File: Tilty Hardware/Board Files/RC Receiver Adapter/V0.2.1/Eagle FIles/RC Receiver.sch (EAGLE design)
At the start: 31 parts, among them U1 ATMEGA328P, U2 LM2931, U3 AP7313SOT23R, Y1 16MHz

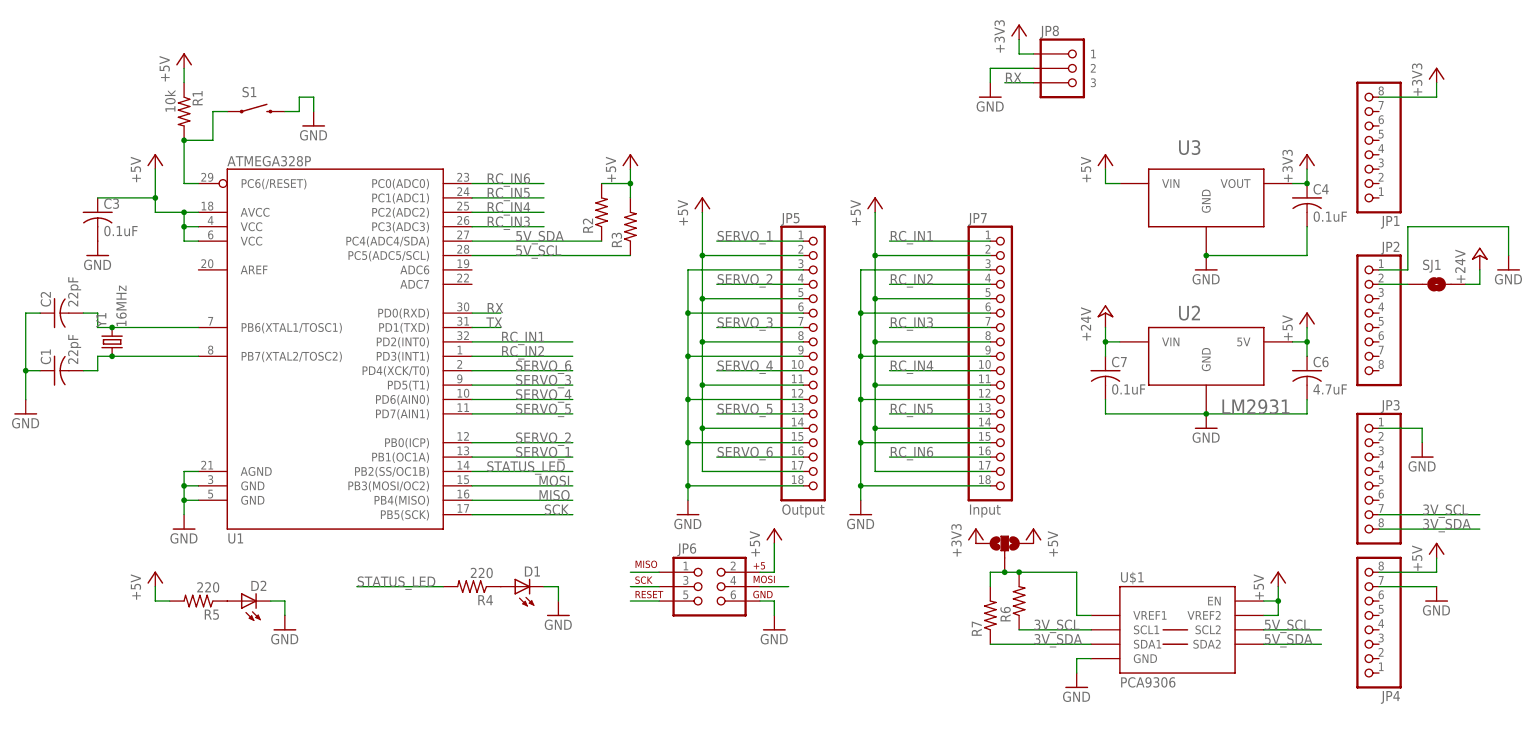
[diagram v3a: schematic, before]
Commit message: Updated RC adapter
Changed to use locking headers, 3v3 I2C line with level
translator/buffer, moved LEDs
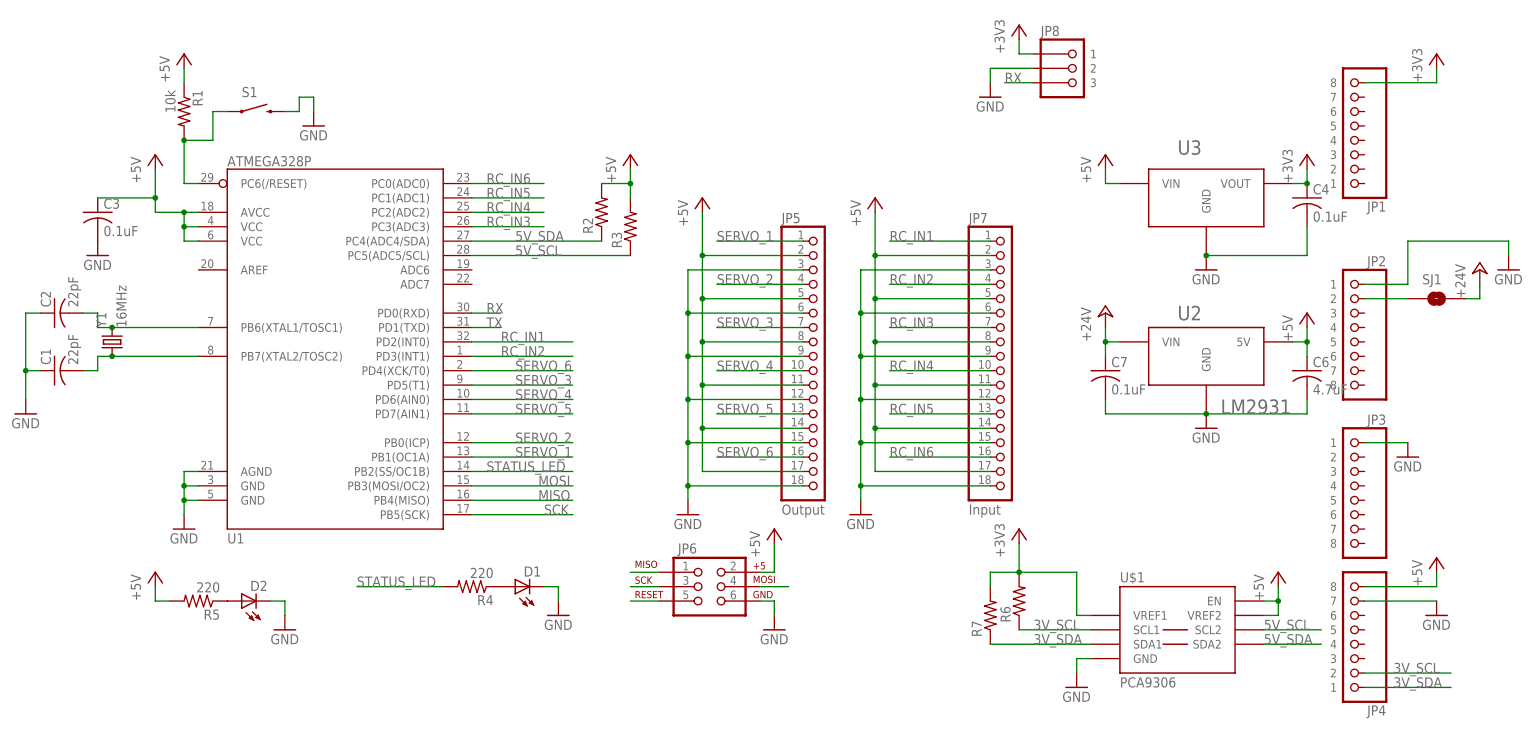
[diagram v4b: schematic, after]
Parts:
- removed SJ2: (no value), SparkFun-Passives:SOLDERJUMPER_2WAYS
- JP1, JP2, JP3, JP4: value (none) -> 8-PIN_HEADER; device pinhead:PINHD-1X81X08_NO_SILK -> My Parts:8-PIN_HEADER
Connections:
- removed net N$7: R6.2, R7.2, SJ2.2, U$1.VREF1
- net +3V3: now also R6.2, R7.2, U$1.VREF1; no longer SJ2.1
- net +5V: no longer SJ2.3
- net 3V_SCL: now also JP4.2; no longer JP3.7
- net 3V_SDA: now also JP4.1; no longer JP3.8
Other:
- moved on the sheet: SJ1

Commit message: Added Tilty silkscreen and option 5/3.3v I2C connections
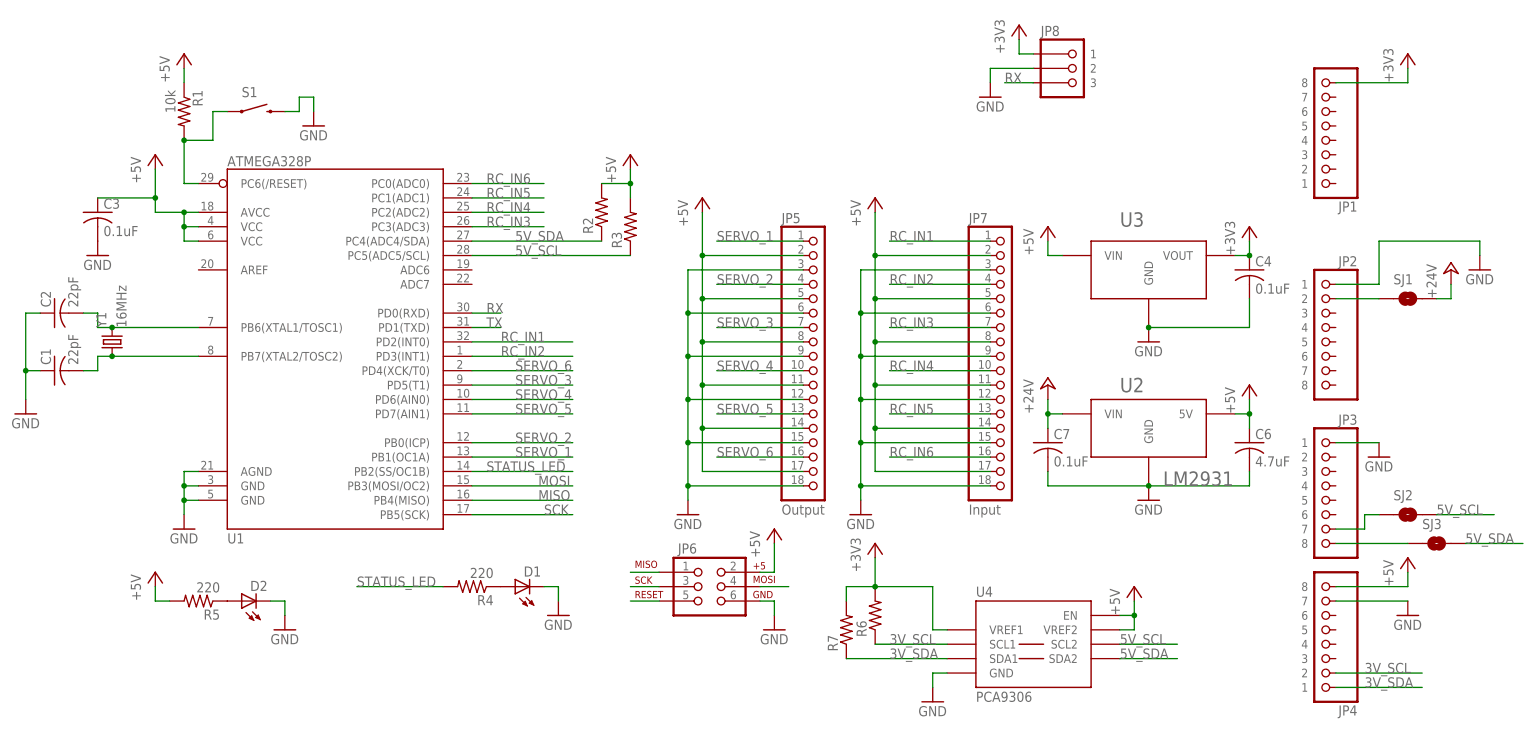
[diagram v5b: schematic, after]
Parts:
- removed U$1: PCA9306, My Parts:PCA9306
- added SJ2, SJ3: SOLDERJUMPERNC2, SparkFun-Passives:SOLDERJUMPERNC2
- added U4: PCA9306, My Parts:PCA9306
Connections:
- new net N$7: JP3.8, SJ3.1
- new net N$8: JP3.7, SJ2.1
- net +3V3: now also U4.VREF1; no longer U$1.VREF1
- net +5V: now also U4.EN, U4.VREF2; no longer U$1.EN, U$1.VREF2
- net 3V_SCL: now also U4.SCL1; no longer U$1.SCL1
- net 3V_SDA: now also U4.SDA1; no longer U$1.SDA1
- net 5V_SCL: now also SJ2.2, U4.SCL2; no longer U$1.SCL2
- net 5V_SDA: now also SJ3.2, U4.SDA2; no longer U$1.SDA2
- net GND: now also U4.GND; no longer U$1.GND
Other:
- moved on the sheet: C4, C6, C7, JP1, JP2, JP3, JP4, R6, R7, SJ1, U2, U3

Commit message: Added serial breakout to R/C adapter
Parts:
- added JP9: (no value), SparkFun-Connectors:M03LOCK
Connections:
- net GND: now also JP9.3
- net RX: now also JP9.2
- net TX: now also JP9.1
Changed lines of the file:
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@@
 <part name="SJ2" library="SparkFun-Passives" deviceset="SOLDERJUMPER" device="NC2"/>
 <part name="SJ3" library="SparkFun-Passives" deviceset="SOLDERJUMPER" device="NC2"/>
+<part name="JP9" library="SparkFun-Connectors" deviceset="M03" device="LOCK"/>
+<part name="GND17" library="supply1" deviceset="GND" device=""/>
 </parts>
 <sheets>
@@
 <attribute name="NAME" x="254" y="40.64" size="1.778" layer="95"/>
 </instance>
+<instance part="JP9" gate="G$1" x="157.48" y="121.92" rot="R180"/>
+<instance part="GND17" gate="1" x="147.32" y="114.3"/>
 </instances>
 <busses>
@@
 <pinref part="GND7" gate="1" pin="GND"/>
 </segment>
+<segment>
+<pinref part="JP9" gate="G$1" pin="3"/>
+<wire x1="149.86" y1="119.38" x2="147.32" y2="119.38" width="0.1524" layer="91"/>
+<pinref part="GND17" gate="1" pin="GND"/>
+<wire x1="147.32" y1="116.84" x2="147.32" y2="119.38" width="0.1524" layer="91"/>
+</segment>
 </net>
 <net name="+24V" class="0">
@@
 <label x="88.9" y="78.74" size="1.778" layer="95"/>
 </segment>
+<segment>
+<pinref part="JP9" gate="G$1" pin="2"/>
+<wire x1="149.86" y1="121.92" x2="142.24" y2="121.92" width="0.1524" layer="91"/>
+</segment>
 </net>
 <net name="+3V3" class="0">
@@
 <label x="88.9" y="76.2" size="1.778" layer="95"/>
 </segment>
-</net>
+<segment>
+<pinref part="JP9" gate="G$1" pin="1"/>
+<wire x1="149.86" y1="124.46" x2="142.24" y2="124.46" width="0.1524" layer="91"/>
+</segment>
+</net>

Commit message: Moved serial breakout slightly
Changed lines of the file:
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@@
 <segment>
 <pinref part="JP9" gate="G$1" pin="2"/>
-<wire x1="149.86" y1="121.92" x2="142.24" y2="121.92" width="0.1524" layer="91"/>
+<wire x1="149.86" y1="121.92" x2="144.78" y2="121.92" width="0.1524" layer="91"/>
+<label x="144.78" y="121.92" size="1.778" layer="95"/>
 </segment>
 </net>
@@
 <segment>
 <pinref part="JP9" gate="G$1" pin="1"/>
-<wire x1="149.86" y1="124.46" x2="142.24" y2="124.46" width="0.1524" layer="91"/>
+<wire x1="149.86" y1="124.46" x2="144.78" y2="124.46" width="0.1524" layer="91"/>
+<label x="144.78" y="124.46" size="1.778" layer="95"/>
 </segment>
 </net>
